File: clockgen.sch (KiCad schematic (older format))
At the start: 32 parts, among them Q1 PMOS, Q10 PMOS, Q11 PMOS, Q12 PMOS, Q13 PMOS, Q14 PMOS, Q15 PMOS, Q16 PMOS, Q17 PMOS, Q18 PMOS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

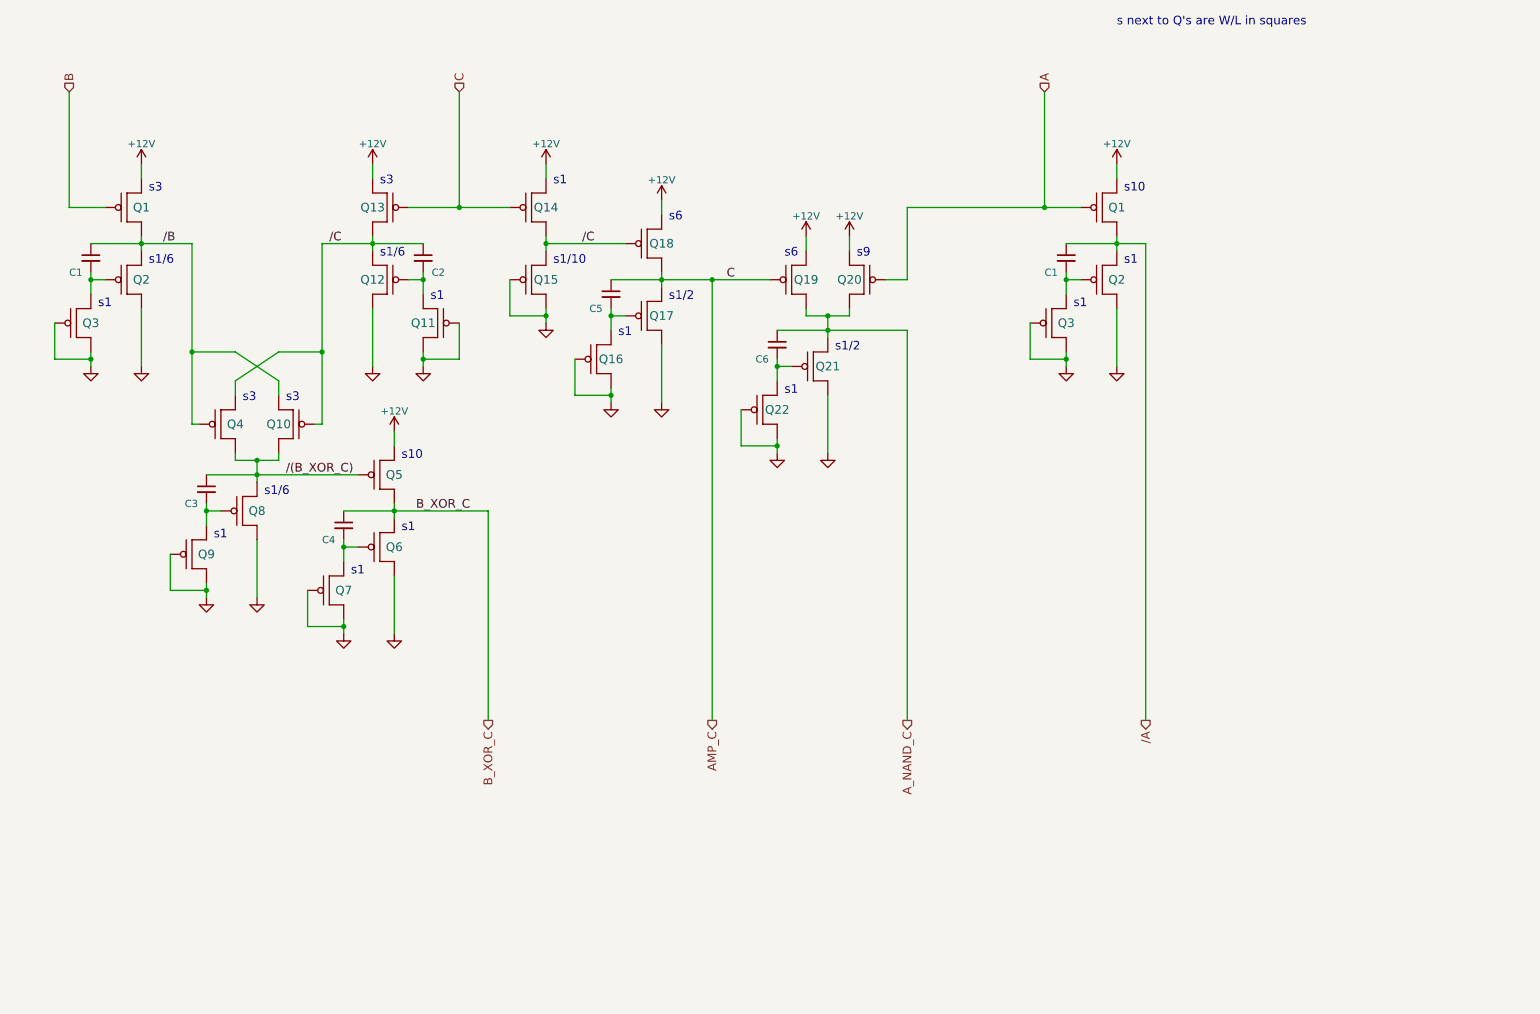
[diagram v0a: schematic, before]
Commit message: Adds clock phase generator schematics and PDFs, adds generic gates to mos.lib
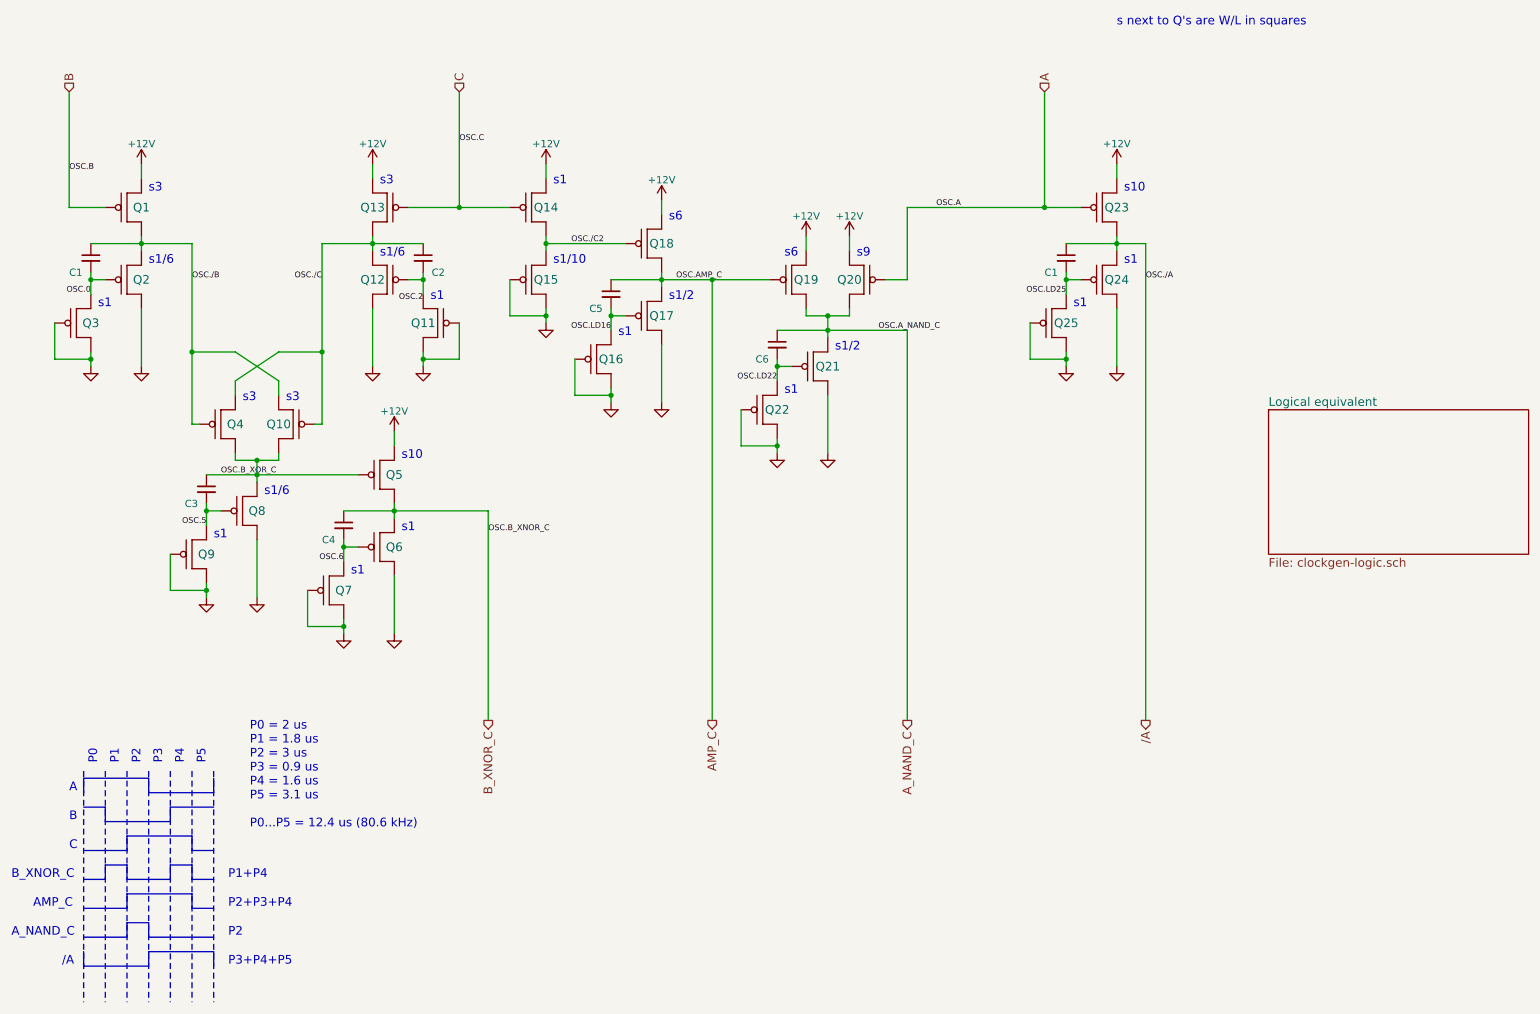
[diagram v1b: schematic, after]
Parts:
- renumbered Q1 to Q23, Q2 to Q24, Q3 to Q25
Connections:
- net AMP_C: no longer Q13.G, Q14.G
- net OSC.LD25: now reaches C1.2, Q24.G, Q25.D
- net OSC.0: now reaches C1.2, Q2.G, Q3.D
- net OSC.5: now reaches C3.2, Q8.G, Q9.D
- net OSC.6: now reaches C4.2, Q6.G, Q7.D
- net OSC.LD16: now reaches C5.2, Q16.D, Q17.G
- net OSC.LD22: now reaches C6.2, Q21.G, Q22.D
- net /(B_XOR_C) renamed OSC.B_XOR_C
- net /B renamed OSC./B
- net /C renamed OSC./C
- net OSC./C: no longer Q14.D, Q15.D, Q18.G
- net B_XOR_C renamed B_XNOR_C
- new net C: Q13.G, Q14.G
- new net OSC./C2: Q14.D, Q15.D, Q18.G
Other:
- note added: "/A"
- note added: "A"
- note added: "AMP_C"
- note added: "A_NAND_C"
- note added: "B"
- note added: "B_XNOR_C"
- note added: "C"
- note added: "P0"
- note added: "P0 = 2 us\nP1 = 1.8 us\nP2 = 3 us\nP3 = 0.9 us\nP4 = 1.6 us\nP5 = 3.1 us\n\nP0...P5 = 12.4 us (80.6 kHz)"
- note added: "P1"
- note added: "P1+P4"
- note added: "P2"
- note added: "P2+P3+P4"
- note added: "P3"
- note added: "P3+P4+P5"
- note added: "P4"
- note added: "P5"
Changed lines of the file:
@@
 $Descr A4 11693 8268
 encoding utf-8
-Sheet 4 7
+Sheet 4 8
 Title ""
 Date ""
@@
 $EndDescr
 $Comp
-L PMOS Q1
+L PMOS Q23
 U 1 1 58897E1B
 P 8050 1900
-F 0 "Q1" H 8150 1900 60  0000 C CNN
+F 0 "Q23" H 8150 1900 60  0000 C CNN
 F 1 "PMOS" H 7950 1350 60  0001 C CNN
 F 2 "" H 8050 1900 60  0001 C CNN
@@
 	8150 2100 8150 2200
 $Comp
-L PMOS Q2
+L PMOS Q24
 U 1 1 58897ED4
 P 8050 2400
-F 0 "Q2" H 8150 2400 60  0000 C CNN
+F 0 "Q24" H 8150 2400 60  0000 C CNN
 F 1 "PMOS" H 7950 1850 60  0001 C CNN
 F 2 "" H 8050 2400 60  0001 C CNN
@@
 $EndComp
 $Comp
-L PMOS Q3
+L PMOS Q25
 U 1 1 58897F0D
 P 7700 2700
-F 0 "Q3" H 7800 2700 60  0000 C CNN
+F 0 "Q25" H 7800 2700 60  0000 C CNN
 F 1 "PMOS" H 7600 2150 60  0001 C CNN
 F 2 "" H 7700 2700 60  0001 C CNN
@@
 Wire Wire Line
 	2350 3650 2350 3600
-Text Label 1550 2150 0    60   ~ 0
-/B
 $Comp
 L PMOS Q13
@@
 Wire Wire Line
 	3000 2600 3000 3000
-Text Label 2700 2150 0    60   ~ 0
-/C
 $Comp
 L PMOS Q8
@@
 	2050 2900 1750 2900
 Connection ~ 1750 2900
-Text Label 2400 3750 0    60   ~ 0
-/(B_XOR_C)
-Text Label 3300 4000 0    60   ~ 0
-B_XOR_C
 Wire Wire Line
 	3800 4000 3800 5450
 Text HLabel 3800 5450 3    60   Output ~ 0
-B_XOR_C
+B_XNOR_C
 $Comp
 L PMOS Q14
@@
 Text HLabel 5350 5450 3    60   Output ~ 0
 AMP_C
-Text Label 4450 2150 0    60   ~ 0
-/C
 $Comp
 L PMOS Q19
@@
 	1    0    0    -1
 $EndComp
-Text Label 5450 2400 0    60   ~ 0
-C
 Wire Wire Line
 	6550 2400 6700 2400
@@
 Text Notes 5850 3200 0    60   ~ 0
 s1
+Text Label 900  1650 0    40   ~ 0
+OSC.B
+Text Label 1050 2500 2    40   ~ 0
+OSC.0
+Text Label 1750 2400 0    40   ~ 0
+OSC./B
+Text Label 3600 1450 0    40   ~ 0
+OSC.C
+Text Label 3350 2550 2    40   ~ 0
+OSC.2
+Text Label 2650 2400 2    40   ~ 0
+OSC./C
+Text Label 1950 3750 0    40   ~ 0
+OSC.B_XOR_C
+Text Label 1850 4100 2    40   ~ 0
+OSC.5
+Text Label 3800 4150 0    40   ~ 0
+OSC.B_XNOR_C
+Text Label 2800 4350 2    40   ~ 0
+OSC.6
+Text Label 4600 2150 2    40   ~ 0
+OSC./C2
+Text Label 4650 2750 2    40   ~ 0
+OSC.LD16
+Text Label 5100 2400 0    40   ~ 0
+OSC.AMP_C
+Text Label 5800 3100 2    40   ~ 0
+OSC.LD22
+Text Label 6900 1900 0    40   ~ 0
+OSC.A
+Text Label 6500 2750 0    40   ~ 0
+OSC.A_NAND_C
+Text Label 7800 2500 2    40   ~ 0
+OSC.LD25
+Text Label 8350 2400 0    40   ~ 0
+OSC./A
+Wire Notes Line
+	1000 5800 1000 7400
+Wire Notes Line
+	1150 5800 1150 7400
+Wire Notes Line
+	1300 5800 1300 7400
+Wire Notes Line
+	1450 5800 1450 7400
+Wire Notes Line
+	1600 5800 1600 7400
+Wire Notes Line
+	1750 5800 1750 7400
+Wire Bus Line
+	1000 5850 1450 5850
+Wire Bus Line
+	1450 5850 1450 5950
+Wire Bus Line
+	1450 5950 1900 5950
+Wire Bus Line
+	1000 5850 1000 5950
+Wire Bus Line
+	1000 6050 1150 6050
+Wire Bus Line
+	1150 6050 1150 6150
+Wire Bus Line
+	1150 6150 1600 6150
+Wire Bus Line
+	1000 6350 1300 6350
+Wire Bus Line
+	1300 6350 1300 6250
+Wire Bus Line
+	1300 6250 1750 6250
+Text Notes 900  5950 0    60   ~ 0
+A
+Text Notes 900  6150 0    60   ~ 0
+B
+Text Notes 900  6350 0    60   ~ 0
+C
+Text Notes 500  6550 0    60   ~ 0
+B_XNOR_C
+Wire Bus Line
+	1000 6550 1150 6550
+Wire Bus Line
+	1150 6550 1150 6450
+Wire Bus Line
+	1150 6450 1300 6450
+Wire Bus Line
+	1300 6450 1300 6550
+Wire Bus Line
+	1300 6550 1600 6550
+Text Notes 650  6750 0    60   ~ 0
+AMP_C
+Wire Bus Line
+	1000 6750 1300 6750
+Wire Bus Line
+	1300 6750 1300 6650
+Wire Bus Line
+	1300 6650 1750 6650
+Text Notes 500  6950 0    60   ~ 0
+A_NAND_C
+Wire Notes Line
+	1900 5800 1900 7400
+Wire Bus Line
+	1900 5950 1900 5850
+Wire Bus Line
+	1600 6150 1600 6050
+Wire Bus Line
+	1600 6050 1900 6050
+Wire Bus Line
+	1750 6250 1750 6350
+Wire Bus Line
+	1750 6350 1900 6350
+Wire Bus Line
+	1600 6550 1600 6450
+Wire Bus Line
+	1600 6450 1750 6450
+Wire Bus Line
+	1750 6450 1750 6550
+Wire Bus Line
+	1750 6550 1900 6550
+Wire Bus Line
+	1750 6650 1750 6750
+Wire Bus Line
+	1750 6750 1900 6750
+Wire Bus Line
+	1000 6950 1300 6950
+Wire Bus Line
+	1300 6950 1300 6850
+Wire Bus Line
+	1300 6850 1450 6850
+Wire Bus Line
+	1450 6850 1450 6950
+Wire Bus Line
+	1450 6950 1900 6950
+Text Notes 850  7150 0    60   ~ 0
+/A
+Wire Bus Line
+	1000 7050 1000 7150
+Wire Bus Line
+	1000 7150 1450 7150
+Wire Bus Line
+	1450 7150 1450 7050
+Wire Bus Line
+	1450 7050 1900 7050
+Wire Bus Line
+	1900 7050 1900 7150
+Text Notes 1100 5750 1    60   ~ 0
+P0
+Text Notes 1250 5750 1    60   ~ 0
+P1
+Text Notes 1400 5750 1    60   ~ 0
+P2
+Text Notes 1550 5750 1    60   ~ 0
+P3
+Text Notes 1700 5750 1    60   ~ 0
+P4
+Text Notes 1850 5750 1    60   ~ 0
+P5
+Text Notes 2150 6200 0    60   ~ 0
+P0 = 2 us\nP1 = 1.8 us\nP2 = 3 us\nP3 = 0.9 us\nP4 = 1.6 us\nP5 = 3.1 us\n\nP0...P5 = 12.4 us (80.6 kHz)
+Text Notes 2000 6550 0    60   ~ 0
+P1+P4
+Text Notes 2000 6750 0    60   ~ 0
+P2+P3+P4
+Text Notes 2000 6950 0    60   ~ 0
+P2
+Text Notes 2000 7150 0    60   ~ 0
+P3+P4+P5
+$Sheet
+S 9200 3300 1800 1000
+U 588EB2A3
+F0 "Logical equivalent" 60
+F1 "clockgen-logic.sch" 60
+$EndSheet
 $EndSCHEMATC
